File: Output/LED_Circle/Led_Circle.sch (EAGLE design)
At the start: 22 parts

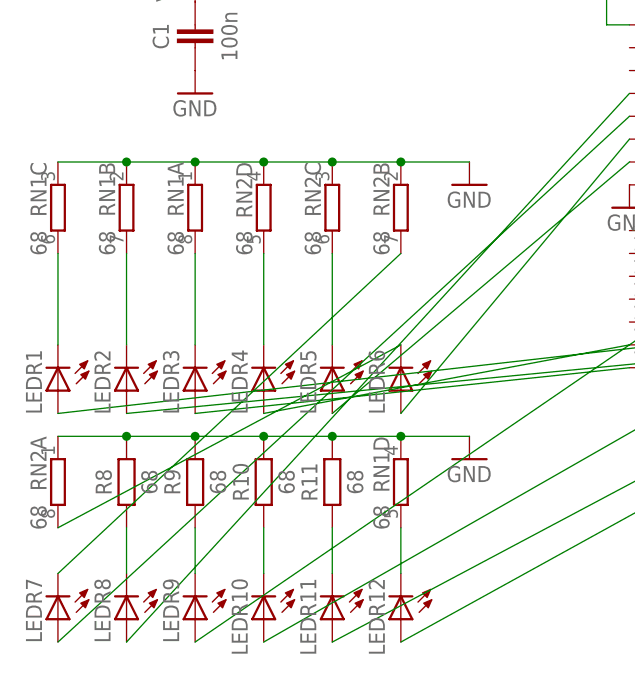
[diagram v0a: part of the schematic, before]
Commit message: Update Pinheader
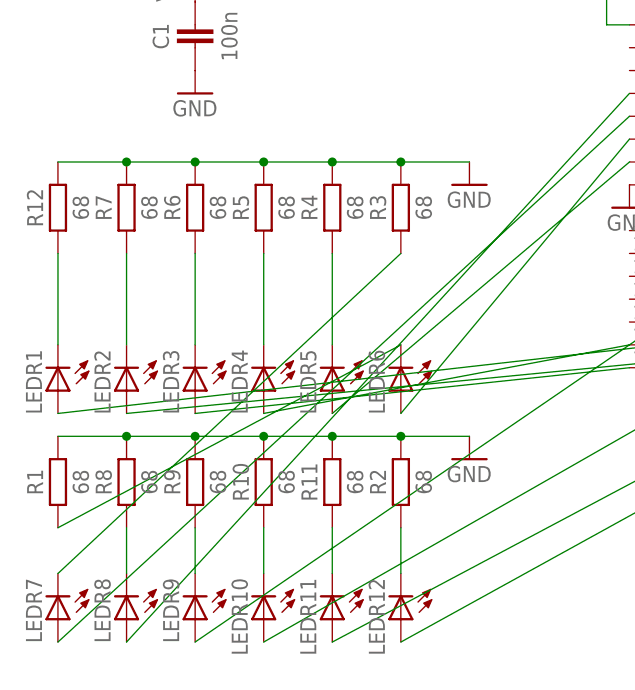
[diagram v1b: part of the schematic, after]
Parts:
- removed RN1, RN2: 68, resistor-dil:4R-N0603-ARC
- added R1, R12, R2, R3, R4, R5, R6, R7: 68, thar:RESISTOR0603
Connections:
- net GND: now also R1.2, R12.2, R2.2, R3.2, R4.2, R5.2, R6.2, R7.2; no longer RN1A.1, RN1B.1, RN1C.1, RN1D.1, RN2A.1, RN2B.1, RN2C.1, RN2D.1
- net N$12: now also R1.1; no longer RN2A.2
- net N$14: now also R4.1; no longer RN2C.2
- net N$15: now also R5.1; no longer RN2D.2
- net N$16: now also R6.1; no longer RN1A.2
- net N$17: now also R7.1; no longer RN1B.2
- net N$18: now also R12.1; no longer RN1C.2
- net N$2: now also R3.1; no longer RN2B.2
- net N$4: now also R2.1; no longer RN1D.2
